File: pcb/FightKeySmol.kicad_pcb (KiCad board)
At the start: 2 copper layers, 168.9 x 83.8 mm, 15 parts, among them U1 Pico

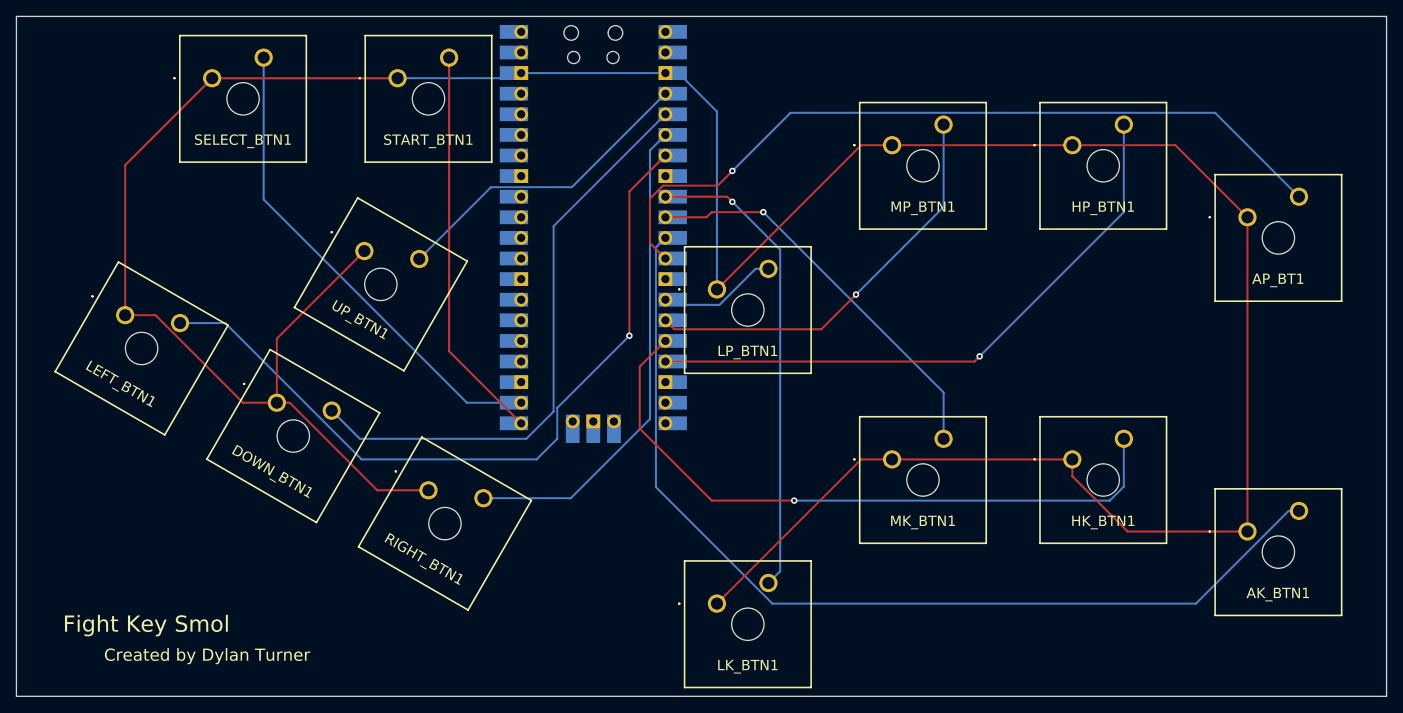
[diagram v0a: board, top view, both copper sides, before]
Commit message: kicad_pcb: shrink board; switch start sel
Signed-off-by: Dylan Turner <dylantdmt@gmail.com>
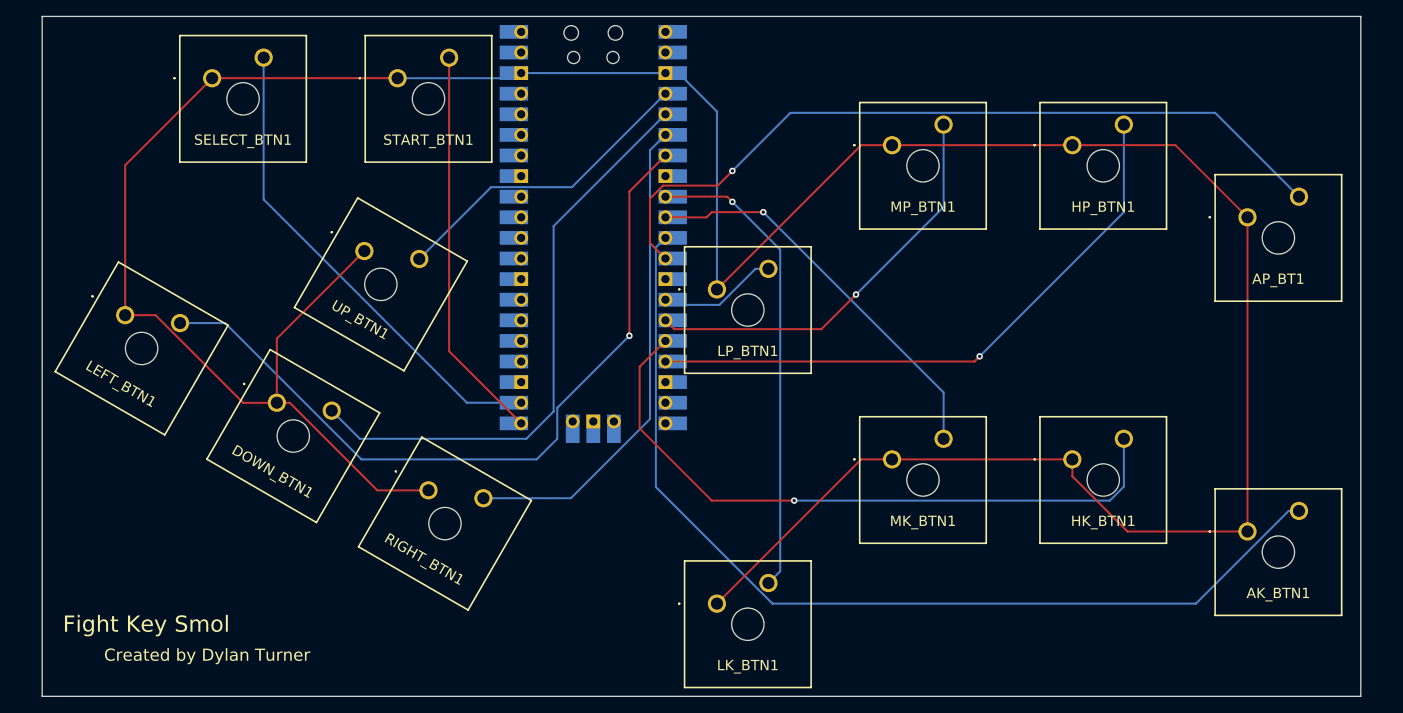
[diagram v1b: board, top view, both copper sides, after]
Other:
- board size 168.9 x 83.8 mm -> 162.6 x 83.8 mm
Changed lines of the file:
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@@
       (net 34 "unconnected-(U1-Pad43)") (pinfunction "SWDIO") (pintype "bidirectional"))
   )
-  (gr_line (start 216.535 50.8) (end 216.535 134.62) (layer "Edge.Cuts") (width 0.05))
-  (gr_line (start 216.535 50.8) (end 47.625 50.8) (layer "Edge.Cuts") (width 0.05))
-  (gr_line (start 47.625 134.62) (end 216.535 134.62) (layer "Edge.Cuts") (width 0.05))
-  (gr_line (start 47.625 134.62) (end 47.625 50.8) (layer "Edge.Cuts") (width 0.05))
+  (gr_line (start 213.36 50.8) (end 213.36 134.62) (layer "Edge.Cuts") (width 0.05))
+  (gr_line (start 213.36 50.8) (end 50.8 50.8) (layer "Edge.Cuts") (width 0.05))
+  (gr_line (start 50.8 134.62) (end 213.36 134.62) (layer "Edge.Cuts") (width 0.05))
+  (gr_line (start 50.8 134.62) (end 50.8 50.8) (layer "Edge.Cuts") (width 0.05))
   (gr_text "Fight Key Smol" (at 53.34 125.73) (layer "F.SilkS")
     (effects (font (size 2 2) (thickness 0.3)) (justify left))
@@
   )
   (dimension (type aligned) (layer "F.Cu")
-    (pts (xy 216.535 50.8) (xy 216.535 134.62))
+    (pts (xy 213.36 50.8) (xy 213.36 134.62))
     (height -6.35)
-    (gr_text "83.8200 mm" (at 221.085 92.71 90) (layer "F.Cu")
+    (gr_text "83.8200 mm" (at 217.91 92.71 90) (layer "F.Cu")
       (effects (font (size 1.5 1.5) (thickness 0.3)))
     )
@@
   )
   (dimension (type aligned) (layer "F.Cu")
-    (pts (xy 47.625 50.8) (xy 216.535 50.8))
+    (pts (xy 50.8 50.8) (xy 213.36 50.8))
     (height -7.62)
-    (gr_text "168.9100 mm" (at 132.08 41.38) (layer "F.Cu")
+    (gr_text "162.5600 mm" (at 132.08 41.38) (layer "F.Cu")
       (effects (font (size 1.5 1.5) (thickness 0.3)))
     )
@@
   (segment (start 125.73 67.31) (end 127.635 65.405) (width 0.25) (layer "B.Cu") (net 36))
   (segment (start 78.105 55.88) (end 78.105 73.365) (width 0.25) (layer "B.Cu") (net 37))
+  (segment (start 78.105 73.365) (end 103.165 98.425) (width 0.25) (layer "B.Cu") (net 37))
   (segment (start 103.165 98.425) (end 109.855 98.425) (width 0.25) (layer "B.Cu") (net 37))
-  (segment (start 78.105 73.365) (end 103.165 98.425) (width 0.25) (layer "B.Cu") (net 37))
+  (segment (start 100.965 55.88) (end 100.965 92.075) (width 0.25) (layer "F.Cu") (net 38))
   (segment (start 100.965 92.075) (end 109.855 100.965) (width 0.25) (layer "F.Cu") (net 38))
-  (segment (start 100.965 55.88) (end 100.965 92.075) (width 0.25) (layer "F.Cu") (net 38))
   (segment (start 116.11 71.85) (end 127.635 60.325) (width 0.25) (layer "B.Cu") (net 41))
   (segment (start 97.291772 80.702806) (end 106.144578 71.85) (width 0.25) (layer "B.Cu") (net 41))

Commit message: kicad_pcb: delete pico, rm traces, shrink board
Signed-off-by: Dylan Turner <dylantdmt@gmail.com>
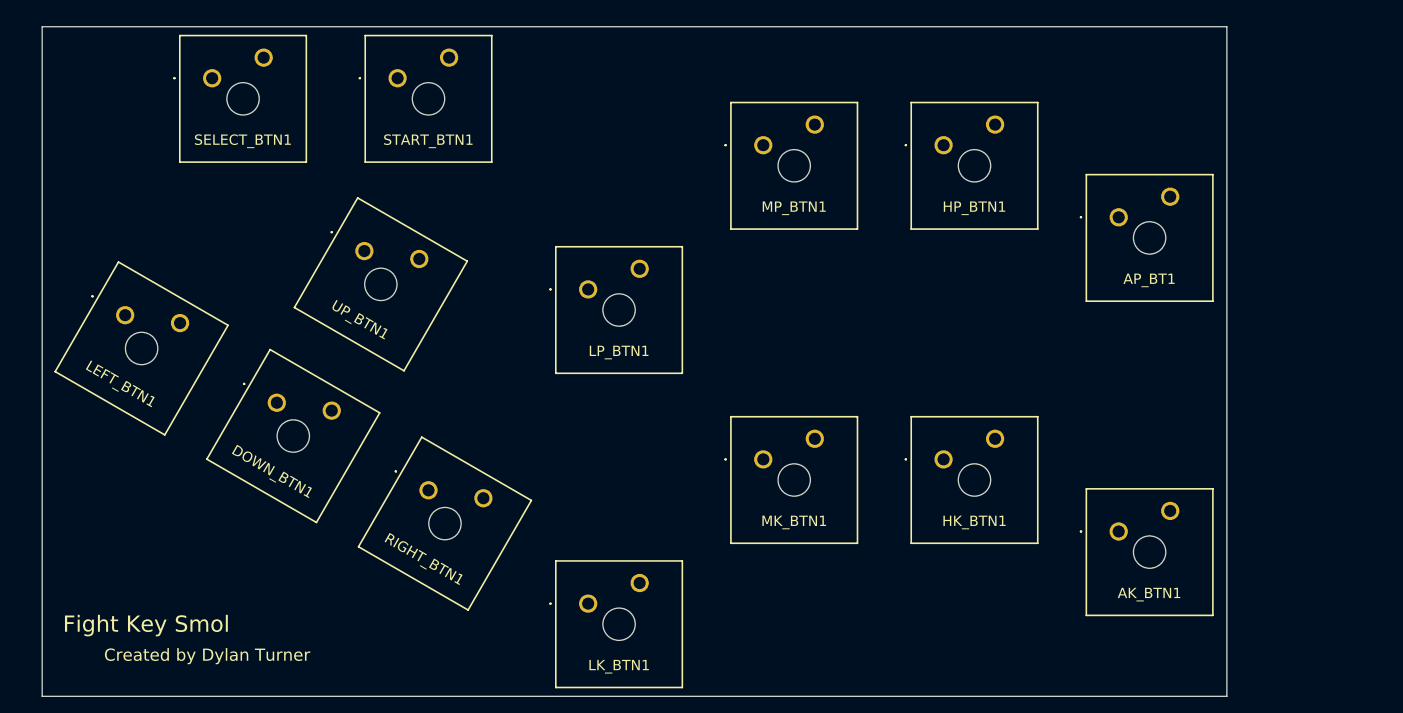
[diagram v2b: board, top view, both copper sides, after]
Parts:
- removed U1: Pico, MCU_RaspberryPi_and_Boards:RPi_Pico_SMD_TH
- moved LK_BTN1 15.9 mm to (118.1, 123.2)
- moved LP_BTN1 15.9 mm to (118.1, 84.5)
- moved AK_BTN1 15.9 mm to (183.5, 114.3)
- moved AP_BT1 15.9 mm to (183.5, 75.6)
- moved HK_BTN1 15.9 mm to (161.9, 105.4)
- moved HP_BTN1 15.9 mm to (161.9, 66.7)
- moved MK_BTN1 15.9 mm to (139.7, 105.4)
- moved MP_BTN1 15.9 mm to (139.7, 66.7)
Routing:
- net /GND: track 382.4 -> 0.00 mm
- net /AK: track 121.2 -> 0.00 mm
- net /AP: track 96.8 -> 0.00 mm, vias 1 -> 0
- net /LEFT: track 95.0 -> 0.00 mm, vias 1 -> 0
- net /HK: track 82.1 -> 0.00 mm, vias 1 -> 0
- net /HP: track 74.9 -> 0.00 mm, vias 1 -> 0
- net /DOWN: track 72.5 -> 0.00 mm
- net /RIGHT: track 60.4 -> 0.00 mm
- net /SELECT: track 59.6 -> 0.00 mm
- net /LK: track 58.5 -> 0.00 mm, vias 1 -> 0
- net /MP: track 51.1 -> 0.00 mm, vias 1 -> 0
- net /MK: track 49.5 -> 0.00 mm, vias 1 -> 0
- net /START: track 48.8 -> 0.00 mm
- net /UP: track 38.8 -> 0.00 mm
- net /LP: track 14.8 -> 0.00 mm
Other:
- board size 162.6 x 83.8 mm -> 146.1 x 82.6 mm

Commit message: kicad_pcb: place and route parts for USB/Power
Signed-off-by: Dylan Turner <dylantdmt@gmail.com>
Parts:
- added C1: 1uF, Capacitor_SMD:C_1210_3225Metric, F.Cu at (127.0, 64.1)
- added C2: 1uF, Capacitor_SMD:C_1210_3225Metric, F.Cu at (121.3, 63.5)
- added D1: D, Diode_SMD:D_SOD-323, F.Cu at (132.1, 63.9)
- added R1: 5k, Resistor_SMD:R_0805_2012Metric, B.Cu at (127.6, 63.9)
- added R2: 5k, Resistor_SMD:R_0805_2012Metric, B.Cu at (132.1, 63.9)
- added R3: 10k, Resistor_SMD:R_0201_0603Metric, F.Cu at (130.8, 73.7)
- added REG1: AP2112K-3.3TRG1, 3.3 Regulator:SOT_RG1_DIO, F.Cu at (130.8, 67.9)
- added USB1: USB-310-B-SU, USB-C:CONN_USB-310-B-SU_HYA, F.Cu at (129.5, 56.5)
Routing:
- net /GND: track 0.00 -> 370.5 mm, vias 0 -> 1
- net /VSys: track 0.00 -> 14.2 mm
- net /3.3V: track 0.00 -> 11.9 mm
- net Net-(R3-Pad2): track 0.00 -> 4.89 mm
- net Net-(USB1-PadB5): track 0.00 -> 3.82 mm, vias 0 -> 1
- net Net-(R2-Pad1): track 0.00 -> 3.30 mm, vias 0 -> 1
- net Net-(USB1-PadB9): track 0.00 -> 2.79 mm

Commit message: kicad_*: finished implementing custom 2040 circuit
Should work and should be able to be placed entirely by manufacturer

Signed-off-by: Dylan Turner <dylantdmt@gmail.com>
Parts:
- added C10: 100nF, Capacitor_SMD:C_0201_0603Metric, F.Cu at (66.3, 112.2)
- added C11: 100nF, Capacitor_SMD:C_0201_0603Metric, F.Cu at (60.6, 118.8)
- added C12: 100nF, Capacitor_SMD:C_0201_0603Metric, F.Cu at (70.4, 112.2)
- added C13: 100nF, Capacitor_SMD:C_0201_0603Metric, F.Cu at (65.5, 112.2)
- added C14: 100nF, Capacitor_SMD:C_0201_0603Metric, F.Cu at (68.9, 112.2)
- added C15: 27pF, Capacitor_SMD:C_0201_0603Metric, F.Cu at (62.0, 132.4)
- added C16: 27pF, Capacitor_SMD:C_0201_0603Metric, F.Cu at (70.4, 132.3)
- added C3: 1uF, Capacitor_SMD:C_0201_0603Metric, F.Cu at (64.7, 104.8)
- added C4: 1uF, Capacitor_SMD:C_0201_0603Metric, F.Cu at (68.6, 107.8)
- added C5: 100nF, Capacitor_SMD:C_0201_0603Metric, F.Cu at (53.0, 110.6)
- added C6: 100nF, Capacitor_SMD:C_0201_0603Metric, F.Cu at (60.3, 115.2)
- added C7: 100nF, Capacitor_SMD:C_0201_0603Metric, F.Cu at (65.7, 123.9)
- added C8: 100nF, Capacitor_SMD:C_0201_0603Metric, F.Cu at (71.9, 118.8)
- added C9: 100nF, Capacitor_SMD:C_0201_0603Metric, F.Cu at (72.5, 115.0)
- added R4: 10k, Resistor_SMD:R_0201_0603Metric, F.Cu at (71.3, 122.5)
- added R5: 27, Resistor_SMD:R_0201_0603Metric, F.Cu at (67.1, 112.2)
- added R6: 27, Resistor_SMD:R_0201_0603Metric, F.Cu at (68.0, 112.2)
- added R7: 10k, Resistor_SMD:R_0201_0603Metric, F.Cu at (57.0, 110.6)
- added R8: 1k, Resistor_SMD:R_0201_0603Metric, F.Cu at (53.2, 114.3)
- added R9: 1k, Resistor_SMD:R_0201_0603Metric, F.Cu at (67.4, 123.5)
- added RDNP1: DNP, Resistor_SMD:R_0201_0603Metric, F.Cu at (62.0, 123.4)
- added SW_BOOT1: SW_Push, Button_Switch_SMD:SW_SPST_PTS645, F.Cu at (115.2, 72.2)
- added U1: RP2040TR7, footprints:RP2040TR7_RPI, F.Cu at (66.1, 117.8)
- added U2: W25Q32JVSSIQ, SPI Flash:SOIC-8_5P28X5P28_WIN, F.Cu at (60.6, 108.0)
- added Y1: Crystal, Crystal:Crystal_SMD_HC49-SD, F.Cu at (66.0, 127.1)
- C1, C2: footprint Capacitor_SMD:C_1210_3225Metric -> Capacitor_SMD:C_0201_0603Metric
- R1, R2: moved to F.Cu
- moved R1 7.60 mm to (122.2, 58.6)
- moved R2 7.16 mm to (136.9, 58.6)
- moved C2 0.84 mm to (121.1, 62.7)
- moved C1 0.61 mm to (127.6, 64.2)
- renumbered AP_BT1 to AP_BTN1
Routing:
- net /AP: track 0.00 -> 196.4 mm, vias 0 -> 8
- net /MP: track 0.00 -> 184.3 mm, vias 0 -> 7
- net /AK: track 0.00 -> 176.9 mm, vias 0 -> 2
- net /HP: track 0.00 -> 173.5 mm, vias 0 -> 4
- net /3.3V: track 11.9 -> 160.6 mm, vias 0 -> 8
- net /USB_N: track 0.00 -> 142.4 mm
- net /USB_P: track 0.00 -> 141.0 mm, vias 0 -> 2
- net /MK: track 0.00 -> 138.4 mm, vias 0 -> 2
- net /HK: track 0.00 -> 131.8 mm, vias 0 -> 2
- net /GND: track 370.5 -> 485.7 mm, vias 1 -> 5
- net /USB_BOOT: track 0.00 -> 104.9 mm, vias 0 -> 4
- net /LK: track 0.00 -> 98.9 mm, vias 0 -> 2
- net /START: track 0.00 -> 82.4 mm, vias 0 -> 2
- net /LP: track 0.00 -> 82.4 mm, vias 0 -> 2
- net /RIGHT: track 0.00 -> 79.7 mm, vias 0 -> 4
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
